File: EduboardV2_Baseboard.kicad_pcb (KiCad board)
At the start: 4 copper layers, 100 x 160 mm, 190 parts, among them IC1 PCF8563T_5,518, IC10 USB2514BI-AEZG-TR, IC2 W25Q128JVSIQTR, IC3 XL1509-5.0E1, IC4 SY8113BADC, IC5 SP3485EN-L_TR, IC8 STK8321, J1 EduboardV2 PCIE UP Board Conn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, J2 Conn_WS2812_Extern, Q1 AO3401A, Q2 AO3400A, Q3 AO3401A, Q4 AO3401A, SW1 1FS1T1B9M2RES-5, SW2 K2-1102SP-C4SC-04, SW3 K2-1102SP-C4SC-04, SW4 K2-1102SP-C4SC-04, SW5 K2-1102SP-C4SC-04, SW6 PEC11R-4220F-S0012, T1 AO3400A, T2 AO3400A, T3 AO3400A, T4 AO3400A, T5 AO3400A, T7 AO3400A, T8 AO3400A, U1 TMP112xxDRL, X1 32.768 kHz, X10 S4B-PH-SM4-K-TB(LF)(SN), X13 KF2EDGR-3.81-3P, X14 CH340G, X15 DSX321G 24MHz, X2 CR1220-2ZX, X3 TF-15×15, X4 KF2EDGR-3.81-3P, X5 DFR0649, X7 BH-00105, X8 USB3.1C16PFSMT, X9 BH-00105, Y1 X322512MSB4SI

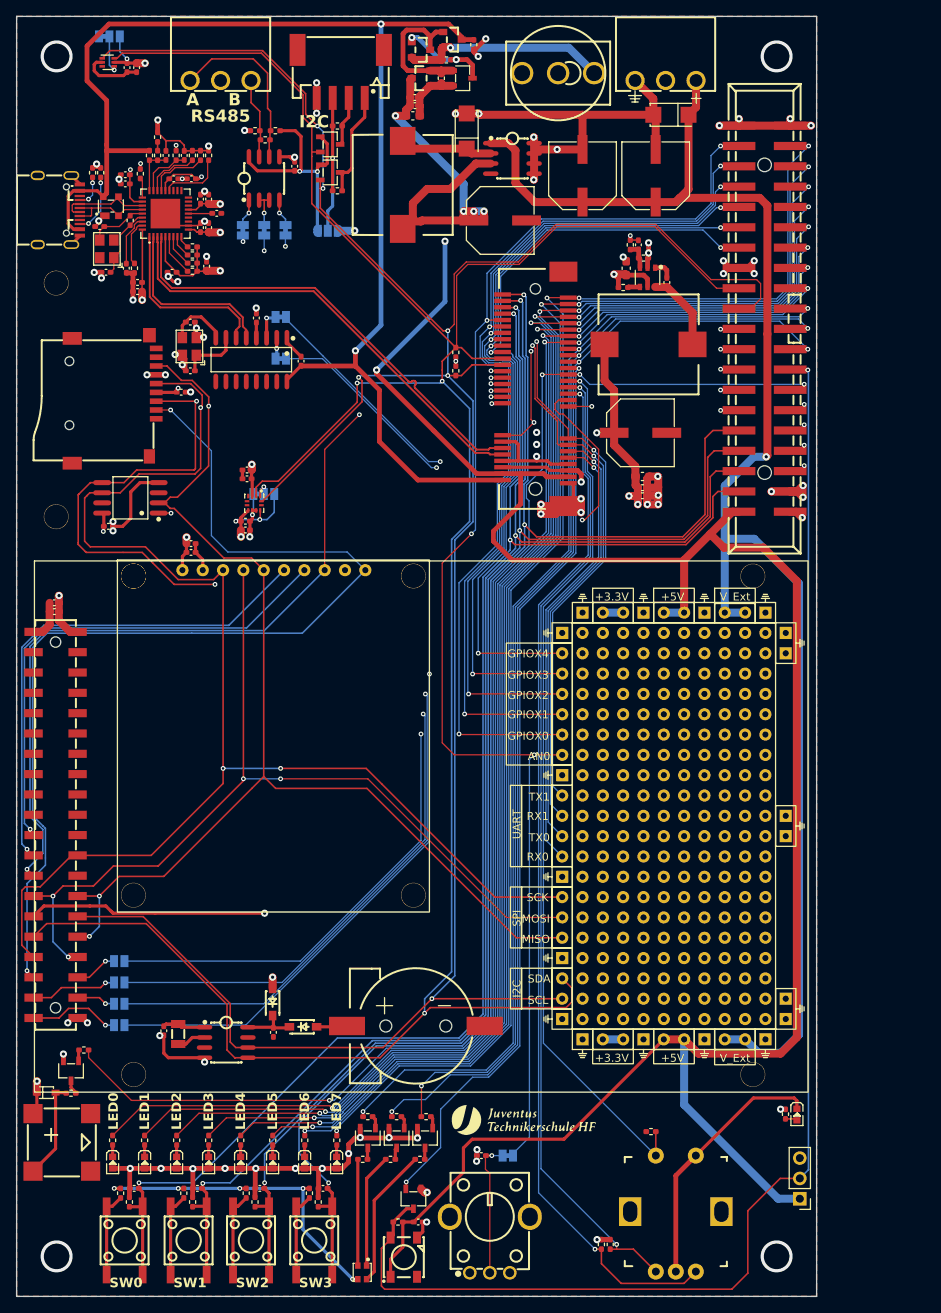
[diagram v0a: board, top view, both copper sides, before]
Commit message: fix parts (like led were wrong way round) Neatify Board
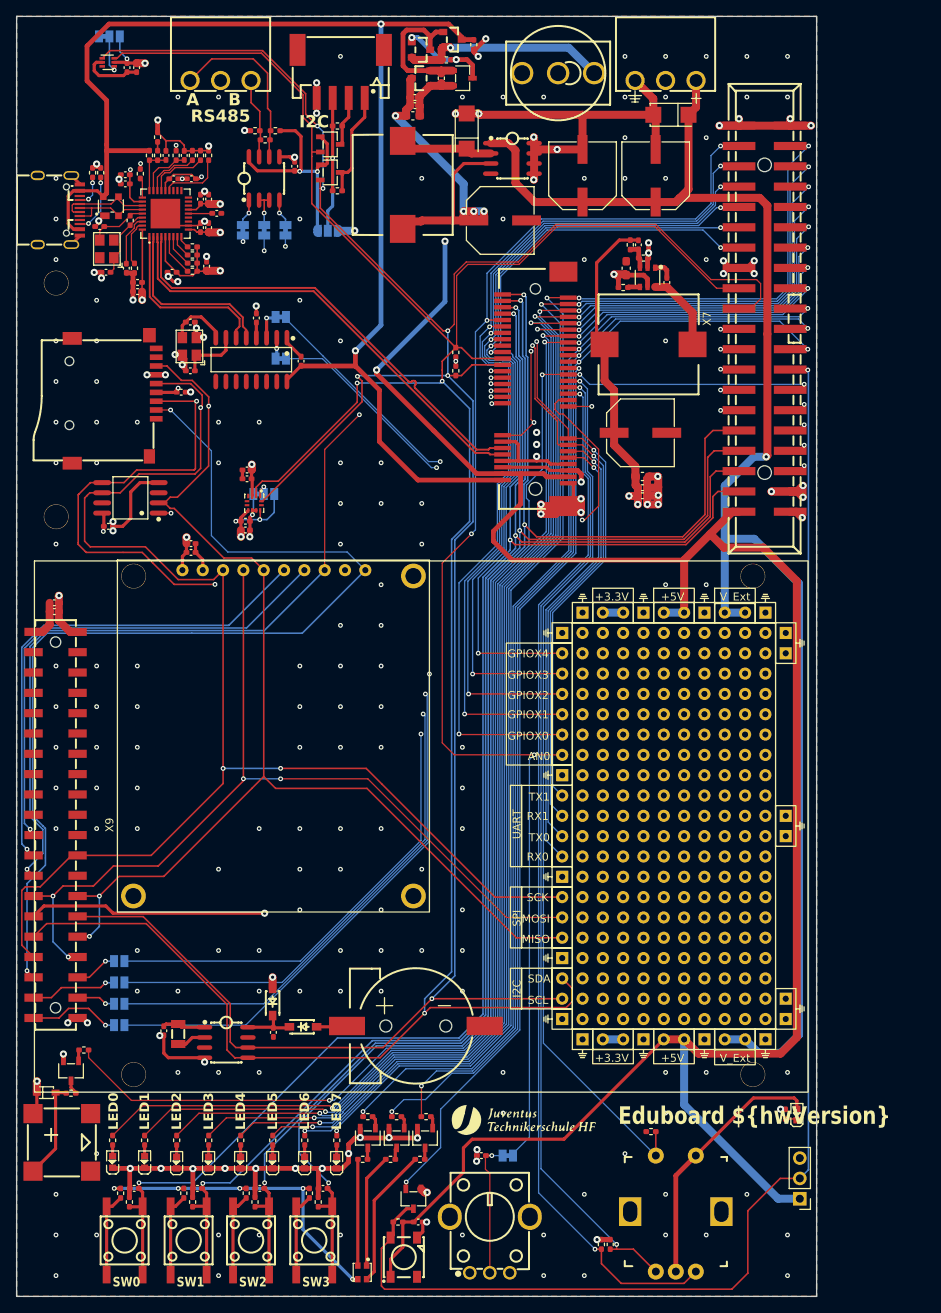
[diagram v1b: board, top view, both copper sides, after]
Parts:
- added G***: LOGO, EduboardV2_kicadlib:logo3, F.Cu at (59.5, 37.7)
- moved D6 0.08 mm to (66.0, 164.2), turned to 90 degrees
- moved D7 0.08 mm to (70.0, 164.2), turned to 90 degrees
- turned D10 to 90 degrees
- turned D11 to 90 degrees
- turned D12 to 90 degrees
- turned D13 to 90 degrees
- turned D5 to 90 degrees
- turned D8 to 90 degrees
- turned D9 to 90 degrees
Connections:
- D10 pad 1: Net-(D10-A) -> GND
- D10 pad 2: GND -> Net-(D10-A)
- D11 pad 1: Net-(D11-A) -> GND
- D11 pad 2: GND -> Net-(D11-A)
- D12 pad 1: Net-(D12-A) -> GND
- D12 pad 2: GND -> Net-(D12-A)
- D13 pad 1: Net-(D13-A) -> GND
- D13 pad 2: GND -> Net-(D13-A)
- D5 pad 1: +3.3V -> Net-(D5-C)
- D5 pad 2: Net-(D5-C) -> +3.3V
- D6 pad 1: Net-(D6-A) -> GND
- D6 pad 2: GND -> Net-(D6-A)
- D7 pad 1: Net-(D7-A) -> GND
- D7 pad 2: GND -> Net-(D7-A)
- D8 pad 1: Net-(D8-A) -> GND
- D8 pad 2: GND -> Net-(D8-A)
- D9 pad 1: Net-(D9-A) -> GND
- D9 pad 2: GND -> Net-(D9-A)
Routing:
- net +3.3V: track 771.2 -> 757.6 mm, vias 36 -> 34
- net +5V_EXT: track 54.7 -> 50.2 mm
- net GND: track 481.5 -> 484.7 mm, vias 83 -> 222
- net WS2812_DIN: track 114.1 -> 112.9 mm
- net PWMR: track 144.1 -> 142.9 mm
- net PWMB: track 141.7 -> 140.5 mm
- net PWMG: track 147.4 -> 146.2 mm
- net (no net): vias 4 -> 0
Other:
- board text added: "Eduboard ${hwVersion}"

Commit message: finalize baseboard. finishing touches
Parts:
- added G***: LOGO, EduboardV2_kicadlib:logo4, F.Cu at (94.0, 106.1)
- added REF**: MountingHole_3.2mm_M3, MountingHole:MountingHole_3.2mm_M3, F.Cu at (59.0, 25.0)
- added REF**: MountingHole_3.2mm_M3, MountingHole:MountingHole_3.2mm_M3, F.Cu at (149.0, 25.0)
- added REF**: MountingHole_3.2mm_M3, MountingHole:MountingHole_3.2mm_M3, F.Cu at (149.0, 175.0)
- added REF**: MountingHole_3.2mm_M3, MountingHole:MountingHole_3.2mm_M3, F.Cu at (59.0, 175.0)
- moved D14 1.79 mm to (97.4, 176.2)
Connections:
- X7 pad 39: GND -> V_EXT
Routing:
- net V_EXT: track 192.3 -> 206.7 mm
- net GND: track 484.7 -> 477.3 mm, vias 222 -> 219
- net SPI0_MISO: track 223.9 -> 228.8 mm
- net Net-(D14-K-Pad2): track 17.5 -> 15.6 mm
- net Net-(D14-K-Pad1): track 14.3 -> 12.4 mm
- net Net-(D14-K-Pad4): track 13.3 -> 11.6 mm
- net TFT_CS: track 108.6 -> 107.1 mm
- net +3.3V: track 757.6 -> 757.1 mm

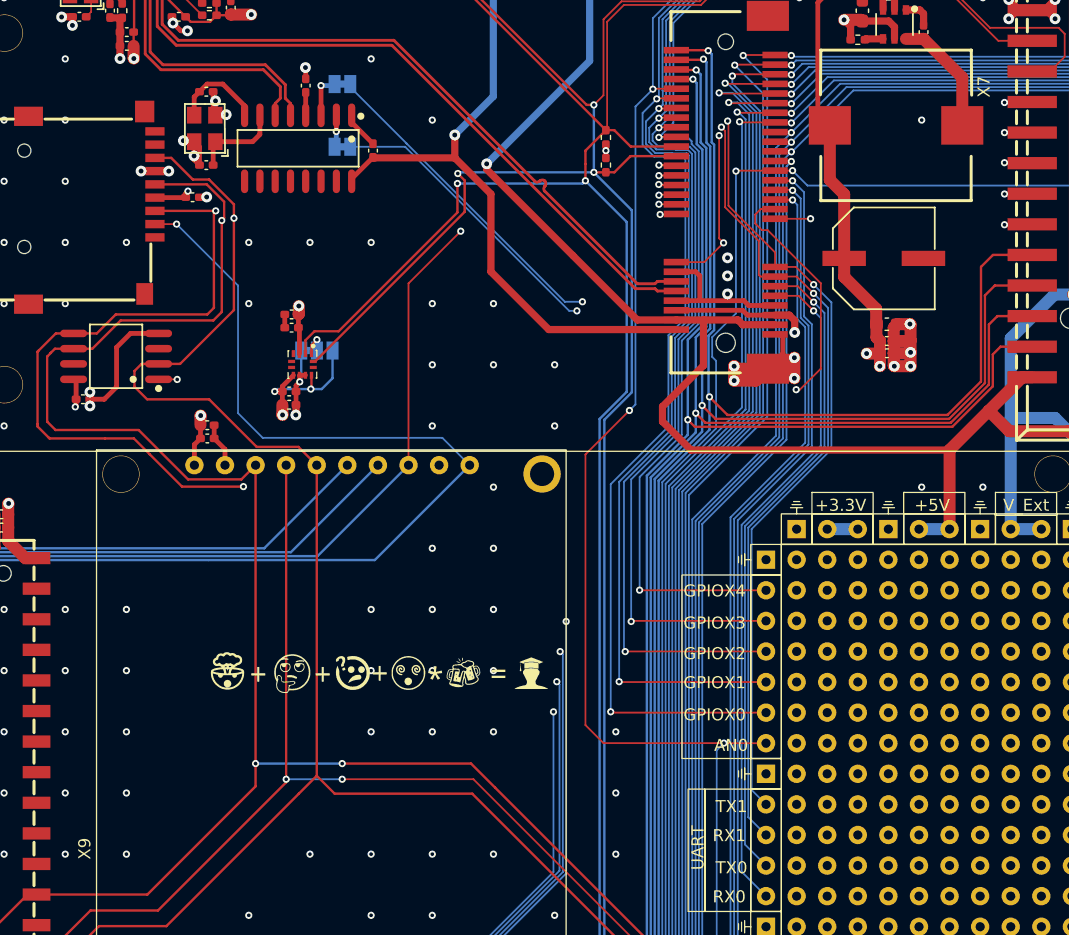
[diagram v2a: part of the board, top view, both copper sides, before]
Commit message: remove some part designators from silkscreen
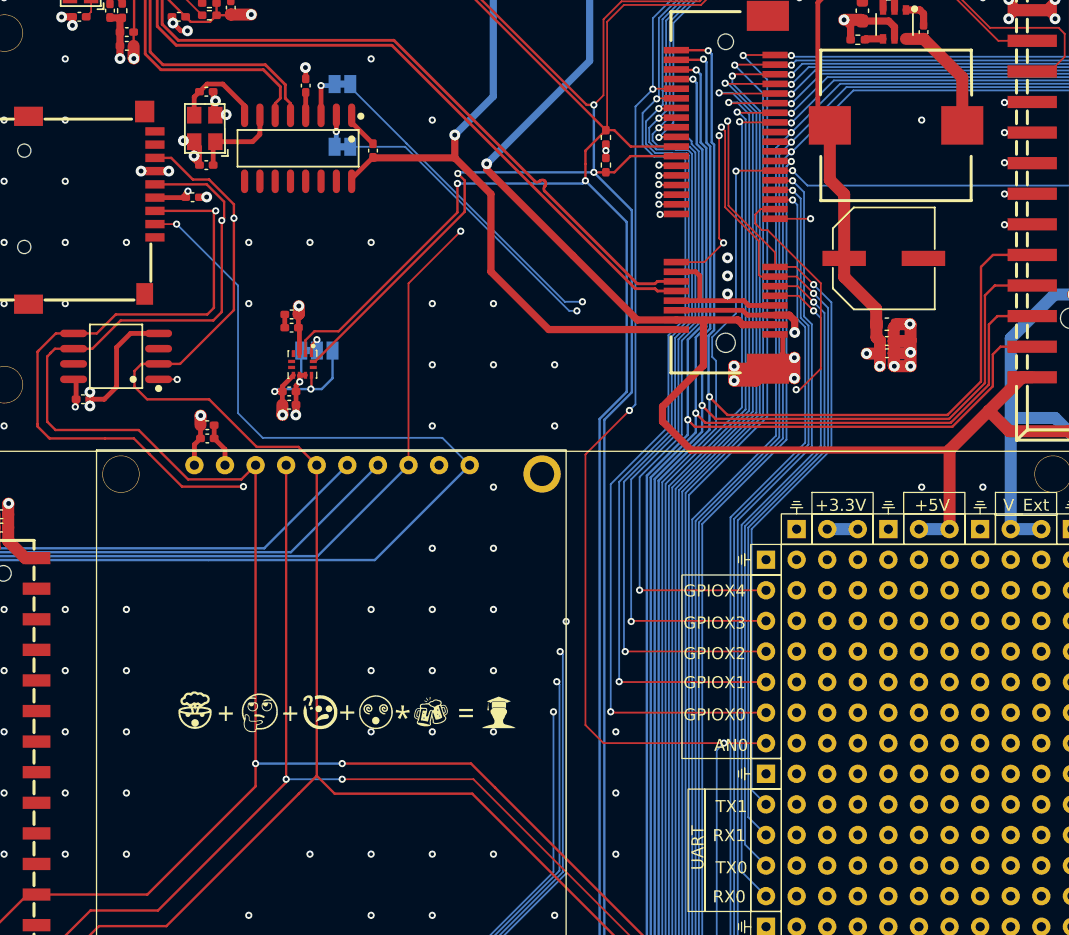
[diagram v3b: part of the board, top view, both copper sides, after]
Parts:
- moved G*** 4.23 mm to (91.3, 109.4)
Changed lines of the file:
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@@
     (property "TouchController Datasheet" "https://www.buydisplay.com/download/ic/FT6236-FT6336-FT6436L-FT6436_Datasheet.pdf")
     (attr smd)
-    (fp_text reference "X9" (at 0 -6.59 90) (layer "F.SilkS")
+    (fp_text reference "X9" (at 0 -6.59 90) (layer "F.SilkS") hide
         (effects (font (size 1 1) (thickness 0.15)))
     )
@@
   )
   (footprint "EduboardV2_kicadlib:logo4" (layer "F.Cu")
-    (at 93.95 106.1)
+    (at 91.253386 109.356432)
     (attr board_only exclude_from_pos_files exclude_from_bom)
     (fp_text reference "G***" (at 0 0) (layer "F.SilkS") hide
@@
     (property "ki_description" "2.54mm -40℃~+105℃ Brick nogging 3A 20 Push - Pull 2.54mm 2 SMD,P=2.54mm  IDC Connectors ROHS")
     (attr smd)
-    (fp_text reference "X7" (at 0 -7.2 90) (layer "F.SilkS")
+    (fp_text reference "X7" (at 0 -7.2 90) (layer "F.SilkS") hide
         (effects (font (size 1 1) (thickness 0.15)))
     )
